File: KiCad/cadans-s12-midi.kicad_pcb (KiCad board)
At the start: 2 copper layers, 19 parts

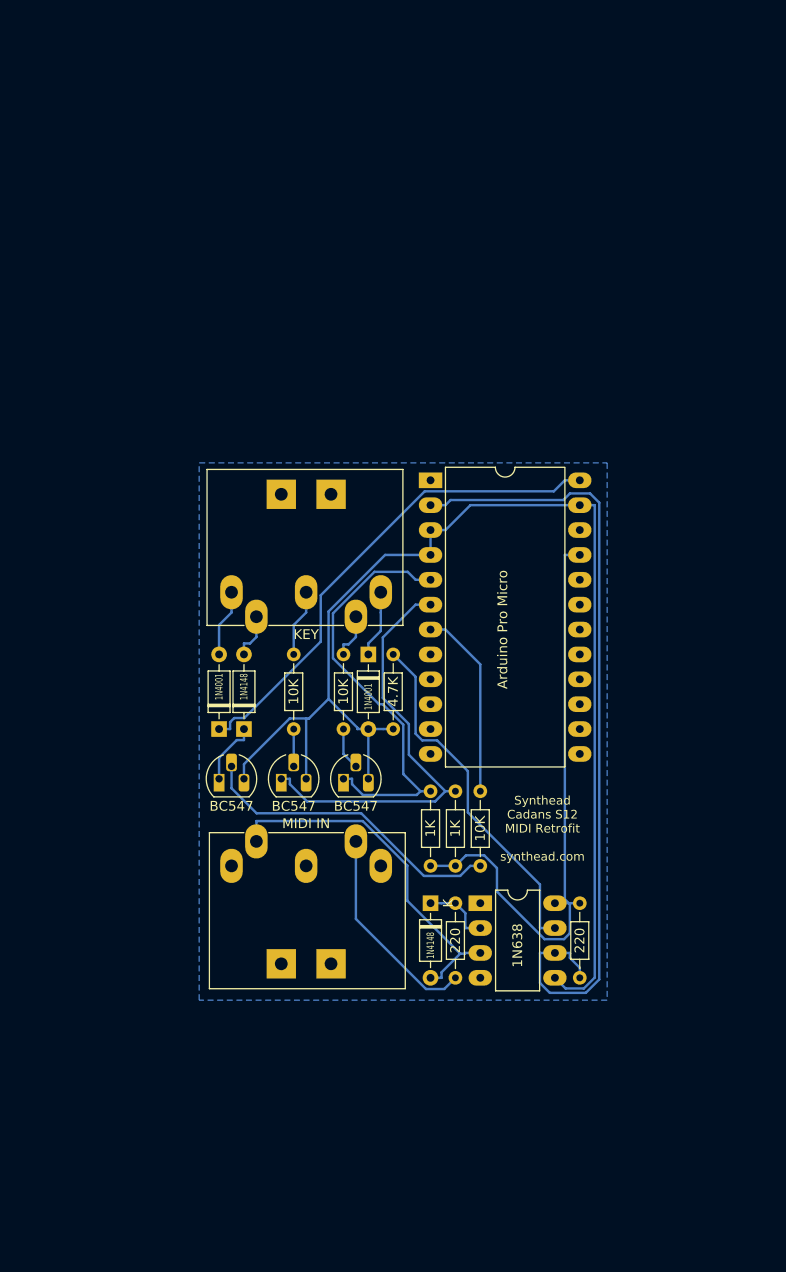
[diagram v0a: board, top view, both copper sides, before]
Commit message: Upadate schematics and PCB for MIDI out and sustain pedal.
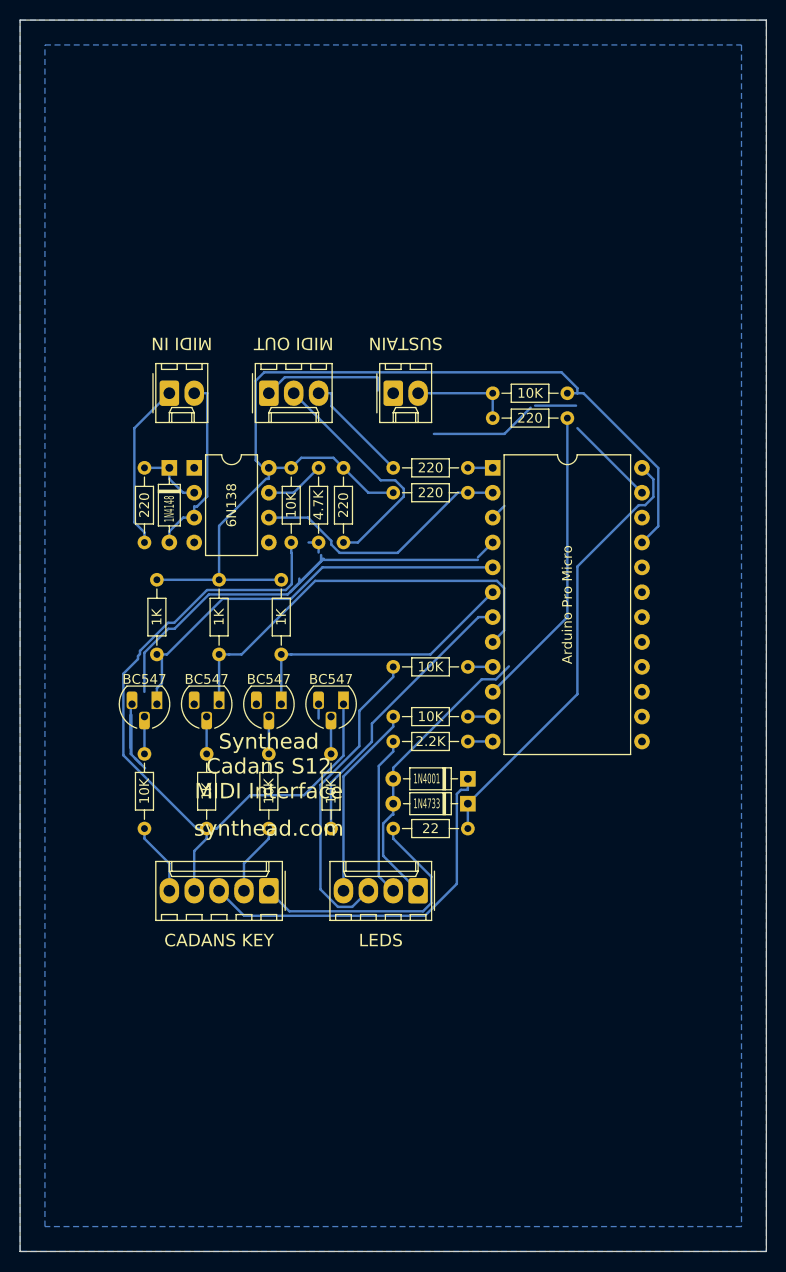
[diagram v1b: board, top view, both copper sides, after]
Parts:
- removed the 10K at (137.2, 102.9)
- removed the 10K at (132.1, 102.9)
- removed the 10K at (151.1, 109.2)
- removed the 1K at (146.1, 116.8)
- removed the 1K at (148.6, 116.8)
- removed the 1N4001 at (124.5, 102.9)
- removed the 1N4001 at (139.7, 95.2)
- removed the 1N4148 at (146.1, 120.7)
- removed the 1N4148 at (127.0, 102.9)
- removed 1N638: 6N138, Package_DIP:DIP-8_W7.62mm_LongPads
- removed the 220 at (148.6, 120.7)
- removed the 220 at (161.3, 120.7)
- removed the BC547 at (137.2, 108.0)
- removed the BC547 at (130.8, 108.0)
- removed the BC547 at (124.5, 108.0)
- removed KEY: Cadans S12 KEY, cadans-s12-midi:SDS-50J
- removed the MIDI IN at (141.0, 116.8)
- added 10K: 10K, Resistor_THT:R_Axial_DIN0204_L3.6mm_D1.6mm_P7.62mm_Horizontal, F.Cu at (116.8, 105.4)
- added 10K: 10K, Resistor_THT:R_Axial_DIN0204_L3.6mm_D1.6mm_P7.62mm_Horizontal, F.Cu at (129.5, 105.4)
- added 10K: 10K, Resistor_THT:R_Axial_DIN0204_L3.6mm_D1.6mm_P7.62mm_Horizontal, F.Cu at (135.9, 113.0)
- added 10K: 10K, Resistor_THT:R_Axial_DIN0204_L3.6mm_D1.6mm_P7.62mm_Horizontal, F.Cu at (131.8, 76.2)
- added 10K: 10K, Resistor_THT:R_Axial_DIN0204_L3.6mm_D1.6mm_P7.62mm_Horizontal, F.Cu at (152.4, 68.6)
- added 10K: 10K, Resistor_THT:R_Axial_DIN0204_L3.6mm_D1.6mm_P7.62mm_Horizontal, F.Cu at (149.9, 96.5)
- added 10K: 10K, Resistor_THT:R_Axial_DIN0204_L3.6mm_D1.6mm_P7.62mm_Horizontal, F.Cu at (149.9, 101.6)
- added 1K: 1K, Resistor_THT:R_Axial_DIN0204_L3.6mm_D1.6mm_P7.62mm_Horizontal, F.Cu at (118.1, 87.6)
- added 1K: 1K, Resistor_THT:R_Axial_DIN0204_L3.6mm_D1.6mm_P7.62mm_Horizontal, F.Cu at (130.8, 87.6)
- added 1K: 1K, Resistor_THT:R_Axial_DIN0204_L3.6mm_D1.6mm_P7.62mm_Horizontal, F.Cu at (123.2, 105.4)
- added 1K: 1K, Resistor_THT:R_Axial_DIN0204_L3.6mm_D1.6mm_P7.62mm_Horizontal, F.Cu at (124.5, 87.6)
- added 1N4001: 1N4001, Diode_THT:D_DO-35_SOD27_P7.62mm_Horizontal, F.Cu at (149.9, 108.0)
- added 1N4148: 1N4148, Diode_THT:D_DO-35_SOD27_P7.62mm_Horizontal, F.Cu at (119.4, 76.2)
- added 1N4733: 1N4733, Diode_THT:D_DO-35_SOD27_P7.62mm_Horizontal, F.Cu at (149.9, 110.5)
- added 2.2K: 2.2K, Resistor_THT:R_Axial_DIN0204_L3.6mm_D1.6mm_P7.62mm_Horizontal, F.Cu at (149.9, 104.1)
- added 22: 22, Resistor_THT:R_Axial_DIN0204_L3.6mm_D1.6mm_P7.62mm_Horizontal, F.Cu at (149.9, 113.0)
- added 220: 220, Resistor_THT:R_Axial_DIN0204_L3.6mm_D1.6mm_P7.62mm_Horizontal, F.Cu at (116.8, 76.2)
- added 220: 220, Resistor_THT:R_Axial_DIN0204_L3.6mm_D1.6mm_P7.62mm_Horizontal, F.Cu at (142.2, 78.7)
- added 220: 220, Resistor_THT:R_Axial_DIN0204_L3.6mm_D1.6mm_P7.62mm_Horizontal, F.Cu at (142.2, 76.2)
- added 220: 220, Resistor_THT:R_Axial_DIN0204_L3.6mm_D1.6mm_P7.62mm_Horizontal, F.Cu at (137.2, 76.2)
- added 220: 220, Resistor_THT:R_Axial_DIN0204_L3.6mm_D1.6mm_P7.62mm_Horizontal, F.Cu at (160.0, 71.1)
- added 6N138: 6N138, Package_DIP:DIP-8_W7.62mm, F.Cu at (121.9, 76.2)
- added BC547: BC547, Package_TO_SOT_THT:TO-92L_HandSolder, F.Cu at (118.1, 100.3)
- added BC547: BC547, Package_TO_SOT_THT:TO-92L_HandSolder, F.Cu at (130.8, 100.3)
- added BC547: BC547, Package_TO_SOT_THT:TO-92L_HandSolder, F.Cu at (137.2, 100.3)
- added BC547: BC547, Package_TO_SOT_THT:TO-92L_HandSolder, F.Cu at (124.5, 100.3)
- added CADANS KEY: KEY, cadans-s12-midi:Molex_KK_254_5, F.Cu at (129.5, 119.4)
- added LEDS: LEDs, cadans-s12-midi:Molex_KK_254_4, F.Cu at (144.8, 119.4)
- added MIDI IN: MIDI in, cadans-s12-midi:Molex_KK_254_2, F.Cu at (119.4, 68.6)
- added MIDI OUT: MIDI out, cadans-s12-midi:Molex_KK_254_3, F.Cu at (129.5, 68.6)
- added SUSTAIN: Sustain, cadans-s12-midi:Molex_KK_254_2, F.Cu at (142.2, 68.6)
- moved 4.7K 20.5 mm to (134.6, 76.2)
- moved Arduino Pro Micro 6.48 mm to (160.0, 88.9)
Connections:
- Arduino Pro Micro pad 1: (no net) -> Net-(R13-Pad2)
- Arduino Pro Micro pad 10: (no net) -> Net-(R16-Pad1)
- Arduino Pro Micro pad 11: (no net) -> Net-(R19-Pad1)
- Arduino Pro Micro pad 12: (no net) -> Net-(R17-Pad1)
- Arduino Pro Micro pad 8: (no net) -> Net-(Q4-Pad1)
- Arduino Pro Micro pad 9: (no net) -> Net-(R18-Pad1)
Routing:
- net Net-(J4-Pad4): track 0.00 -> 74.8 mm
- net Net-(R8-Pad2): track 82.9 -> 27.1 mm
- net Net-(Q4-Pad1): track 0.00 -> 43.6 mm
- net +5V: track 62.7 -> 106.1 mm
- net Net-(D2-Pad1): track 0.00 -> 38.3 mm
- net Net-(J10-Pad3): track 0.00 -> 32.1 mm
- net Net-(R16-Pad1): track 0.00 -> 31.1 mm
- net Net-(R7-Pad1): track 36.6 -> 6.13 mm
- net Net-(Q3-Pad2): track 31.8 -> 3.81 mm
- net Net-(J4-Pad1): track 0.00 -> 27.0 mm
- net Net-(J12-Pad2): track 0.00 -> 24.2 mm
- net Net-(J1-Pad4): track 21.5 -> 0.00 mm
- net Net-(J10-Pad4): track 0.00 -> 19.9 mm
- net Net-(D1-Pad2): track 37.1 -> 19.0 mm
- net Net-(J5-Pad1): track 0.00 -> 17.1 mm
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- added copper zone on B.Cu, net (none)
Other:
- board outline added: 76.2 x 125.7 mm
- net class Default: clearance 0.2286 -> 0.2; trace_width 0.2286 -> 0.25
- rule pad_to_mask_clearance: 0.05 -> 0
- rule trace_clearance: 0.2286 -> 0.2
- board text added: "Reserved for chassis conectors"
- board text added: "Synthead Cadans S12 MIDI Interface"
- board text added: "synthead.com"
- board text removed: "Synthead Cadans S12 MIDI Retrofit synthead.com"

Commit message: Fix broken GNDREF connection to the 6N138 optocoupler.
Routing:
- net GNDREF: track 138.2 -> 140.7 mm
